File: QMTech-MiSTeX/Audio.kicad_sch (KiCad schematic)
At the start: 16 parts, among them CN1 PJ-327A 5JJ, J9 Conn_01x06_Male, U5 ZGY133/T10(PLT)

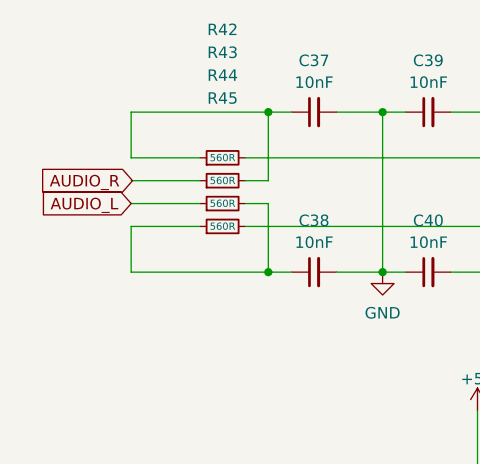
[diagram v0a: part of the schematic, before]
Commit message: add UART connections
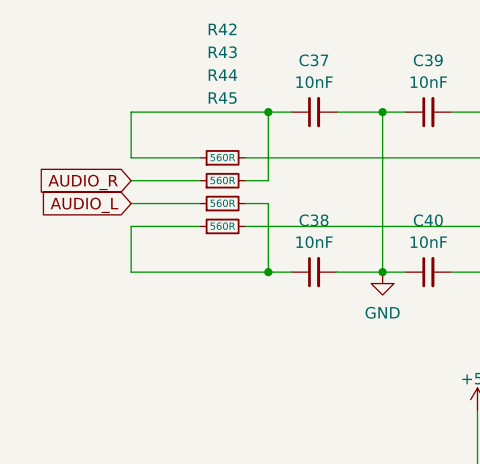
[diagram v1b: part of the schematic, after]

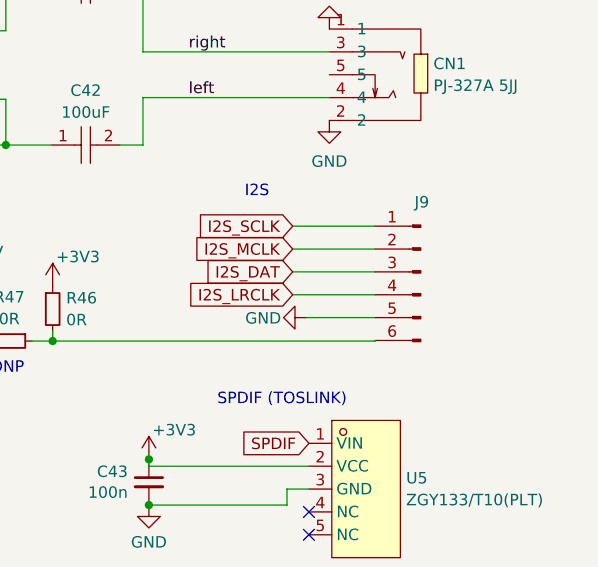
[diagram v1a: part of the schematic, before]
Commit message: QMTech-MiSTeX: make I2S audio to the DVI optional, use SPDIF by default
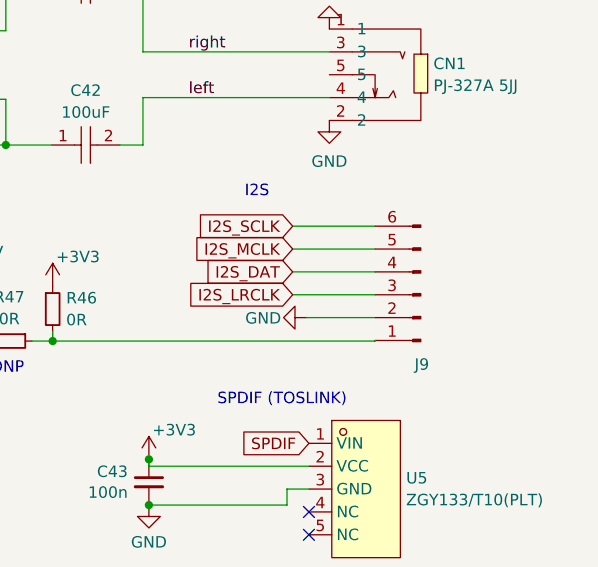
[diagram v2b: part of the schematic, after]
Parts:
- J9: footprint Connector_PinHeader_2.54mm:PinHeader_1x06_P2.54mm_Vertical -> Connector_PinSocket_2.54mm:PinSocket_1x06_P2.54mm_Horizontal
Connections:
- net GND: now also J9.2 (Pin_2); no longer J9.5 (Pin_5)
- net I2S_DAT: now also J9.4 (Pin_4); no longer J9.3 (Pin_3)
- net I2S_LRCLK: now also J9.3 (Pin_3); no longer J9.4 (Pin_4)
- net I2S_MCLK: now also J9.5 (Pin_5); no longer J9.2 (Pin_2)
- net I2S_SCLK: now also J9.6 (Pin_6); no longer J9.1 (Pin_1)
- net at R46.2, R47.1: now also J9.1 (Pin_1); no longer J9.6 (Pin_6)
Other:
- moved on the sheet: J9
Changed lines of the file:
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@@
     )
   )
-  (symbol (lib_id "Connector:Conn_01x06_Male") (at 197.104 112.014 0) (mirror y) (unit 1)
+  (symbol (lib_id "Connector:Conn_01x06_Male") (at 197.104 114.554 180) (unit 1)
     (in_bom yes) (on_board yes) (dnp no)
-    (property "Reference" "J9" (at 197.231 104.267 0)
+    (property "Reference" "J9" (at 197.231 122.301 0)
       (effects (font (size 1.27 1.27)))
     )
-    (property "Value" "Conn_01x06_Male" (at 197.1421 104.2185 0)
+    (property "Value" "Conn_01x06_Male" (at 197.1421 122.3495 0)
       (effects (font (size 1.27 1.27)) hide)
     )
-    (property "Footprint" "Connector_PinHeader_2.54mm:PinHeader_1x06_P2.54mm_Vertical" (at 197.104 112.014 0)
+    (property "Footprint" "Connector_PinSocket_2.54mm:PinSocket_1x06_P2.54mm_Horizontal" (at 197.104 114.554 0)
       (effects (font (size 1.27 1.27)) hide)
     )
-    (property "Datasheet" "~" (at 197.104 112.014 0)
+    (property "Datasheet" "~" (at 197.104 114.554 0)
       (effects (font (size 1.27 1.27)) hide)
     )

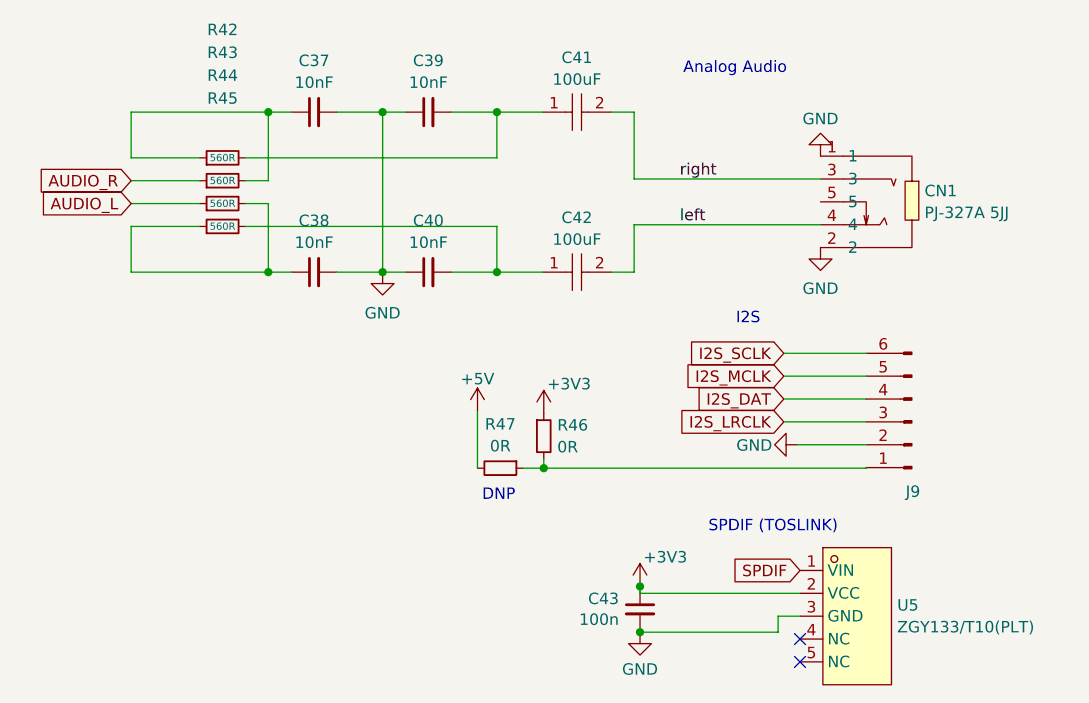
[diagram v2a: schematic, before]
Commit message: finish routing/layouting, fix silk screen, add mounting holes
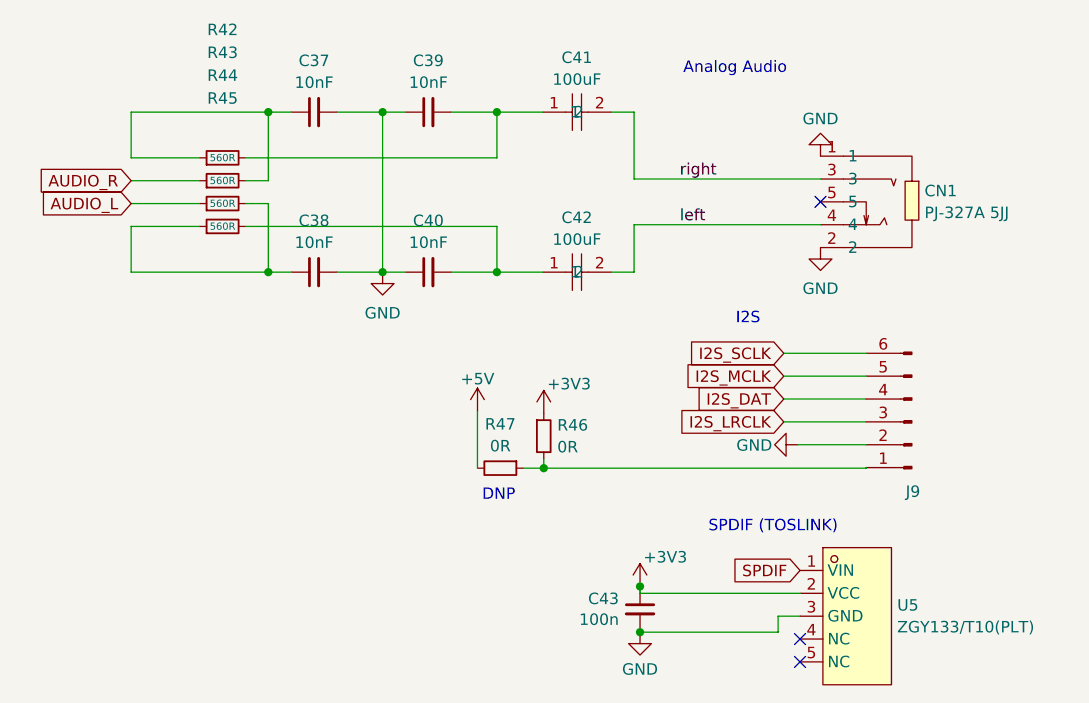
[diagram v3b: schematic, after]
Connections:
- no-connect marks 2 -> 3
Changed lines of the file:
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@@
   (junction (at 138.303 97.917) (diameter 0) (color 0 0 0 0)
   )
+  (no_connect (at 186.9575 90.1079))
   (no_connect (at 184.6834 141.224))
   (no_connect (at 184.6834 138.684))
@@
     )
   )
-  (symbol (lib_id "easyeda2kicad:CL31A107MQHNNNE") (at 159.893 97.917 0) (unit 1)
+  (symbol (lib_name "CL31A107MQHNNNE_1") (lib_id "easyeda2kicad:CL31A107MQHNNNE") (at 159.893 97.917 0) (unit 1)
     (in_bom yes) (on_board yes) (dnp no) (fields_autoplaced)
     (property "Reference" "C42" (at 159.893 91.8697 0)
@@
       (project "QMTech-MiSTeX"
         (path "/bf95850e-2fcb-4784-a603-f17fc357556b/1e65a514-c552-4463-908f-afe88949be5c"
-          (reference "#PWR0141") (unit 1)
+          (reference "#PWR0138") (unit 1)
         )
       )
@@
       (project "QMTech-MiSTeX"
         (path "/bf95850e-2fcb-4784-a603-f17fc357556b/1e65a514-c552-4463-908f-afe88949be5c"
-          (reference "#PWR0139") (unit 1)
+          (reference "#PWR0142") (unit 1)
         )
       )
@@
       (project "QMTech-MiSTeX"
         (path "/bf95850e-2fcb-4784-a603-f17fc357556b/1e65a514-c552-4463-908f-afe88949be5c"
-          (reference "J9") (unit 1)
+          (reference "J11") (unit 1)
         )
       )
@@
       (project "QMTech-MiSTeX"
         (path "/bf95850e-2fcb-4784-a603-f17fc357556b/1e65a514-c552-4463-908f-afe88949be5c"
-          (reference "R45") (unit 1)
+          (reference "R50") (unit 1)
         )
       )
@@
       (project "QMTech-MiSTeX"
         (path "/bf95850e-2fcb-4784-a603-f17fc357556b/1e65a514-c552-4463-908f-afe88949be5c"
-          (reference "#PWR0135") (unit 1)
+          (reference "#PWR0139") (unit 1)
         )
       )
@@
       (project "QMTech-MiSTeX"
         (path "/bf95850e-2fcb-4784-a603-f17fc357556b/1e65a514-c552-4463-908f-afe88949be5c"
-          (reference "#PWR0140") (unit 1)
+          (reference "#PWR0143") (unit 1)
         )
       )
@@
       (project "QMTech-MiSTeX"
         (path "/bf95850e-2fcb-4784-a603-f17fc357556b/1e65a514-c552-4463-908f-afe88949be5c"
-          (reference "R42") (unit 1)
+          (reference "R47") (unit 1)
         )
       )
@@
       (project "QMTech-MiSTeX"
         (path "/bf95850e-2fcb-4784-a603-f17fc357556b/1e65a514-c552-4463-908f-afe88949be5c"
-          (reference "R47") (unit 1)
+          (reference "R51") (unit 1)
         )
       )
@@
       (project "QMTech-MiSTeX"
         (path "/bf95850e-2fcb-4784-a603-f17fc357556b/1e65a514-c552-4463-908f-afe88949be5c"
-          (reference "R44") (unit 1)
+          (reference "R49") (unit 1)
         )
       )
@@
       (project "QMTech-MiSTeX"
         (path "/bf95850e-2fcb-4784-a603-f17fc357556b/1e65a514-c552-4463-908f-afe88949be5c"
-          (reference "#PWR0142") (unit 1)
+          (reference "#PWR0137") (unit 1)
         )
       )
@@
       (project "QMTech-MiSTeX"
         (path "/bf95850e-2fcb-4784-a603-f17fc357556b/1e65a514-c552-4463-908f-afe88949be5c"
-          (reference "R46") (unit 1)
+          (reference "R52") (unit 1)
         )
       )
@@
       (project "QMTech-MiSTeX"
         (path "/bf95850e-2fcb-4784-a603-f17fc357556b/1e65a514-c552-4463-908f-afe88949be5c"
-          (reference "R43") (unit 1)
+          (reference "R48") (unit 1)
         )
       )
@@
       (project "QMTech-MiSTeX"
         (path "/bf95850e-2fcb-4784-a603-f17fc357556b/1e65a514-c552-4463-908f-afe88949be5c"
-          (reference "#PWR0137") (unit 1)
+          (reference "#PWR0141") (unit 1)
         )
       )
@@
       (project "QMTech-MiSTeX"
         (path "/bf95850e-2fcb-4784-a603-f17fc357556b/1e65a514-c552-4463-908f-afe88949be5c"
+          (reference "#PWR0140") (unit 1)
+        )
+      )
+    )
+  )
+  (symbol (lib_id "power:GND") (at 138.303 97.917 0) (unit 1)
+    (in_bom yes) (on_board yes) (dnp no) (fields_autoplaced)
+    (property "Reference" "#PWR0134" (at 138.303 104.267 0)
+      (effects (font (size 1.27 1.27)) hide)
+    )
+    (property "Value" "GND" (at 138.303 102.4796 0)
+      (effects (font (size 1.27 1.27)))
+    )
+    (property "Footprint" "" (at 138.303 97.917 0)
+      (effects (font (size 1.27 1.27)) hide)
+    )
+    (property "Datasheet" "" (at 138.303 97.917 0)
+      (effects (font (size 1.27 1.27)) hide)
+    )
+    (pin "1")
+    (instances
+      (project "Audio"
+        (path "/40894532-c7c4-4c7b-a6a8-096cd4259f73"
+          (reference "#PWR0134") (unit 1)
+        )
+      )
+      (project "QMTech-MiSTeX"
+        (path "/bf95850e-2fcb-4784-a603-f17fc357556b/1e65a514-c552-4463-908f-afe88949be5c"
           (reference "#PWR0136") (unit 1)
         )
       )
-    )
-  )
-  (symbol (lib_id "power:GND") (at 138.303 97.917 0) (unit 1)
-    (in_bom yes) (on_board yes) (dnp no) (fields_autoplaced)
-    (property "Reference" "#PWR0134" (at 138.303 104.267 0)
-      (effects (font (size 1.27 1.27)) hide)
-    )
-    (property "Value" "GND" (at 138.303 102.4796 0)
-      (effects (font (size 1.27 1.27)))
-    )
-    (property "Footprint" "" (at 138.303 97.917 0)
-      (effects (font (size 1.27 1.27)) hide)
-    )
-    (property "Datasheet" "" (at 138.303 97.917 0)
-      (effects (font (size 1.27 1.27)) hide)
-    )
-    (pin "1")
-    (instances
-      (project "Audio"
-        (path "/40894532-c7c4-4c7b-a6a8-096cd4259f73"
-          (reference "#PWR0134") (unit 1)
-        )
-      )
-      (project "QMTech-MiSTeX"
-        (path "/bf95850e-2fcb-4784-a603-f17fc357556b/1e65a514-c552-4463-908f-afe88949be5c"
-          (reference "#PWR0134") (unit 1)
-        )
-      )

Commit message: fix DRC errors and some warnings too
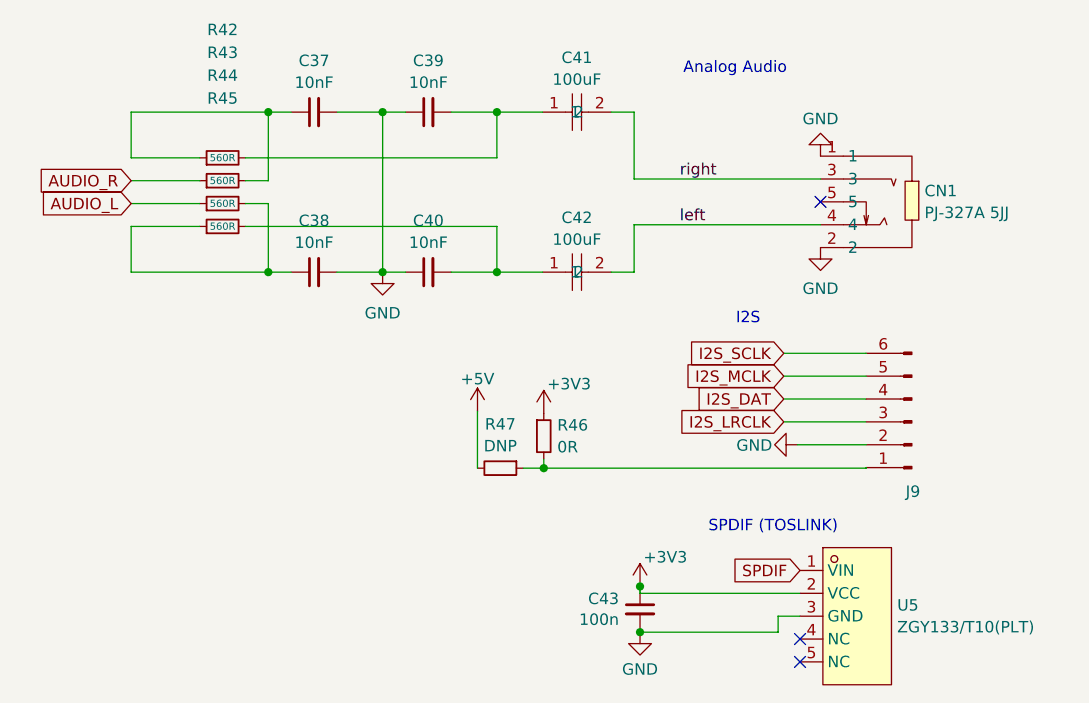
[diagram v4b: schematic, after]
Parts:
- R47: value 0R -> DNP
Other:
- note removed: "DNP"
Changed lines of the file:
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@@
-    (effects (font (size 1.27 1.27)) (justify left bottom))
-  )
-  (text "DNP" (at 149.352 123.5087 0)
     (effects (font (size 1.27 1.27)) (justify left bottom))
   )
@@
       (effects (font (size 1.27 1.27)))
     )
-    (property "Value" "0R" (at 151.384 117.242 90)
+    (property "Value" "DNP" (at 151.384 117.242 90)
       (effects (font (size 1.27 1.27)))
     )
@@
       (effects (font (size 1.27 1.27)) hide)
     )
-    (property "Datasheet" "https://datasheet.lcsc.com/szlcsc/Uniroyal-Elec-0402WGF0000TCE_C17168.pdf" (at 151.384 119.6987 90)
-      (effects (font (size 1.27 1.27)) hide)
-    )
+    (property "Datasheet" "" (at 151.384 119.6987 90)
+      (effects (font (size 1.27 1.27)) hide)
+    )

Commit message: QMTech-MiSTeX WIP
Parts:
- removed R46: 0R, R_0402_1005Metric, symbol jlcpcb-basic-resistor-0402:0R
- removed R47: DNP, R_0402_1005Metric, symbol jlcpcb-basic-resistor-0402:0R
- added R51: DNP, R_0603_1608Metric, symbol jlcpcb-basic-resistor-0603:0R
- added R52: 0R, R_0603_1608Metric, symbol jlcpcb-basic-resistor-0603:0R
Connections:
- net +3V3: now also R52.2
- net +5V: now also R51.1
- net at J9.1 (Pin_1): now also R51.2, R52.1
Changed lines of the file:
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@@
-    )
-  )
-  (symbol (lib_id "jlcpcb-basic-resistor-0402:0R") (at 151.384 119.6987 270) (unit 1)
-    (in_bom yes) (on_board yes) (dnp no) (fields_autoplaced)
-    (property "Reference" "R47" (at 151.384 114.8178 90)
-      (effects (font (size 1.27 1.27)))
-    )
-    (property "Value" "DNP" (at 151.384 117.242 90)
-      (effects (font (size 1.27 1.27)))
-    )
-    (property "Footprint" "R_0402_1005Metric" (at 151.384 117.9207 90)
-      (effects (font (size 1.27 1.27)) hide)
-    )
-    (property "Datasheet" "" (at 151.384 119.6987 90)
-      (effects (font (size 1.27 1.27)) hide)
-    )
-    (pin "1")
-    (pin "2")
-    (instances
-      (project "Audio"
-        (path "/40894532-c7c4-4c7b-a6a8-096cd4259f73"
-          (reference "R47") (unit 1)
-        )
-      )
-      (project "QMTech-MiSTeX"
-        (path "/bf95850e-2fcb-4784-a603-f17fc357556b/1e65a514-c552-4463-908f-afe88949be5c"
-          (reference "R51") (unit 1)
-        )
-      )
     )
   )
@@
     )
   )
-  (symbol (lib_id "jlcpcb-basic-resistor-0402:0R") (at 156.21 116.1427 0) (unit 1)
-    (in_bom yes) (on_board yes) (dnp no) (fields_autoplaced)
-    (property "Reference" "R46" (at 157.7086 114.9306 0)
-      (effects (font (size 1.27 1.27)) (justify left))
-    )
-    (property "Value" "0R" (at 157.7086 117.3548 0)
-      (effects (font (size 1.27 1.27)) (justify left))
-    )
-    (property "Footprint" "R_0402_1005Metric" (at 154.432 116.1427 90)
-      (effects (font (size 1.27 1.27)) hide)
-    )
-    (property "Datasheet" "https://datasheet.lcsc.com/szlcsc/Uniroyal-Elec-0402WGF0000TCE_C17168.pdf" (at 156.21 116.1427 90)
-      (effects (font (size 1.27 1.27)) hide)
-    )
-    (property "LCSC" "C17168" (at 156.21 116.1427 90)
-      (effects (font (size 1.27 1.27)) hide)
-    )
-    (pin "1")
-    (pin "2")
-    (instances
-      (project "Audio"
-        (path "/40894532-c7c4-4c7b-a6a8-096cd4259f73"
-          (reference "R46") (unit 1)
-        )
-      )
-      (project "QMTech-MiSTeX"
-        (path "/bf95850e-2fcb-4784-a603-f17fc357556b/1e65a514-c552-4463-908f-afe88949be5c"
-          (reference "R52") (unit 1)
-        )
-      )
-    )
-  )
   (symbol (lib_id "jlcpcb-basic-resistor-0603:560R") (at 120.523 87.757 90) (unit 1)
     (in_bom yes) (on_board yes) (dnp no)
@@
     )
   )
+  (symbol (lib_id "jlcpcb-basic-resistor-0603:0R") (at 156.21 116.1427 180) (unit 1)
+    (in_bom yes) (on_board yes) (dnp no) (fields_autoplaced)
+    (property "Reference" "R52" (at 157.7086 114.9306 0)
+      (effects (font (size 1.27 1.27)) (justify right))
+    )
+    (property "Value" "0R" (at 157.7086 117.3548 0)
+      (effects (font (size 1.27 1.27)) (justify right))
+    )
+    (property "Footprint" "R_0603_1608Metric" (at 157.988 116.1427 90)
+      (effects (font (size 1.27 1.27)) hide)
+    )
+    (property "Datasheet" "https://datasheet.lcsc.com/szlcsc/Uniroyal-Elec-0603WAF0000T5E_C21189.pdf" (at 156.21 116.1427 90)
+      (effects (font (size 1.27 1.27)) hide)
+    )
+    (property "LCSC" "C21189" (at 156.21 116.1427 90)
+      (effects (font (size 1.27 1.27)) hide)
+    )
+    (pin "2")
+    (pin "1")
+    (instances
+      (project "QMTech-MiSTeX"
+        (path "/bf95850e-2fcb-4784-a603-f17fc357556b/1e65a514-c552-4463-908f-afe88949be5c"
+          (reference "R52") (unit 1)
+        )
+      )
+    )
+  )
   (symbol (lib_id "power:GND") (at 184.404 117.094 270) (mirror x) (unit 1)
     (in_bom yes) (on_board yes) (dnp no)
@@
         )
       )
+    )
+  )
+  (symbol (lib_id "jlcpcb-basic-resistor-0603:0R") (at 151.384 119.6987 90) (unit 1)
+    (in_bom yes) (on_board yes) (dnp no) (fields_autoplaced)
+    (property "Reference" "R51" (at 151.384 114.8178 90)
+      (effects (font (size 1.27 1.27)))
+    )
+    (property "Value" "DNP" (at 151.384 117.242 90)
+      (effects (font (size 1.27 1.27)))
+    )
+    (property "Footprint" "R_0603_1608Metric" (at 151.384 121.4767 90)
+      (effects (font (size 1.27 1.27)) hide)
+    )
+    (property "Datasheet" "https://datasheet.lcsc.com/szlcsc/Uniroyal-Elec-0603WAF0000T5E_C21189.pdf" (at 151.384 119.6987 90)
+      (effects (font (size 1.27 1.27)) hide)
+    )
+    (property "LCSC" "C21189" (at 151.384 119.6987 90)
+      (effects (font (size 1.27 1.27)) hide)
+    )
+    (pin "2")
+    (pin "1")
+    (instances
+      (project "QMTech-MiSTeX"
+        (path "/bf95850e-2fcb-4784-a603-f17fc357556b/1e65a514-c552-4463-908f-afe88949be5c"
+          (reference "R51") (unit 1)
+        )
+      )

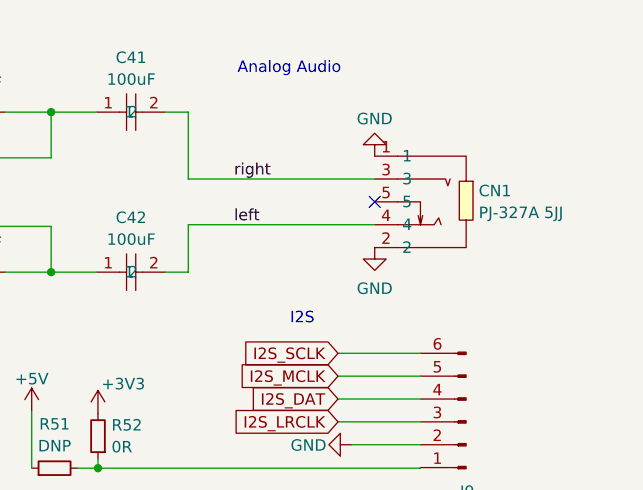
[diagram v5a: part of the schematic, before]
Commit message: power filtering, testpoints, bottom caps, more decoupling, teardrops
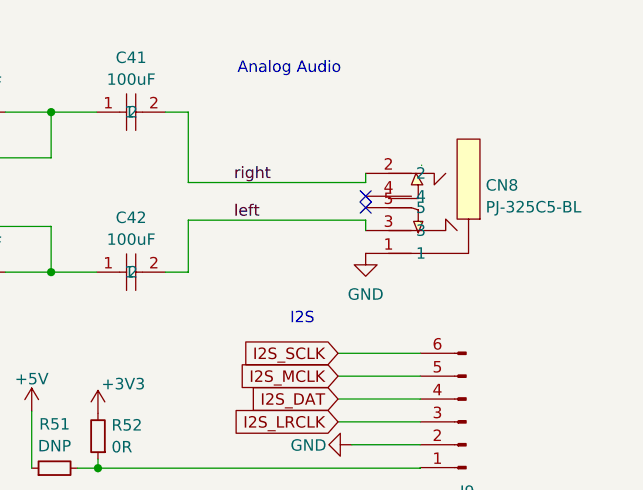
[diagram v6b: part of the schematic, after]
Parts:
- removed CN1: PJ-327A 5JJ, easyeda2kicad:AUDIO-SMD_PJ-327A5JJ, symbol easyeda2kicad:PJ-327A5JJ
- added CN8: PJ-325C5-BL, easyeda2kicad:TH_PJ-325C5-B, symbol easyeda2kicad:PJ-325C5-BL
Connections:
- net GND: now also CN8.1
- net left: now also CN8.3
- net right: now also CN8.2
- no-connect marks 3 -> 4
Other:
- title: (none) -> Audio Output
